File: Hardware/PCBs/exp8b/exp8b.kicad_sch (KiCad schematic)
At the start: 6 parts, among them J1 Conn_01x06_Female, J2 Conn_01x02_Female, U1 7410, U2 7410, U3 7410, U4 7400

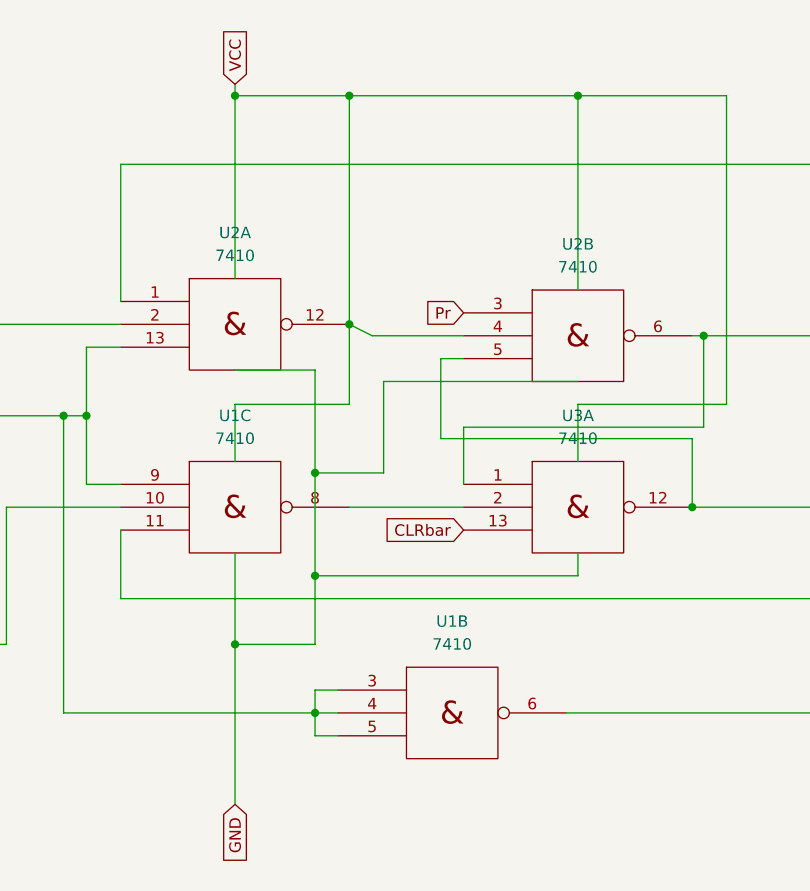
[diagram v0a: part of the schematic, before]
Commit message: Several PCBs updated
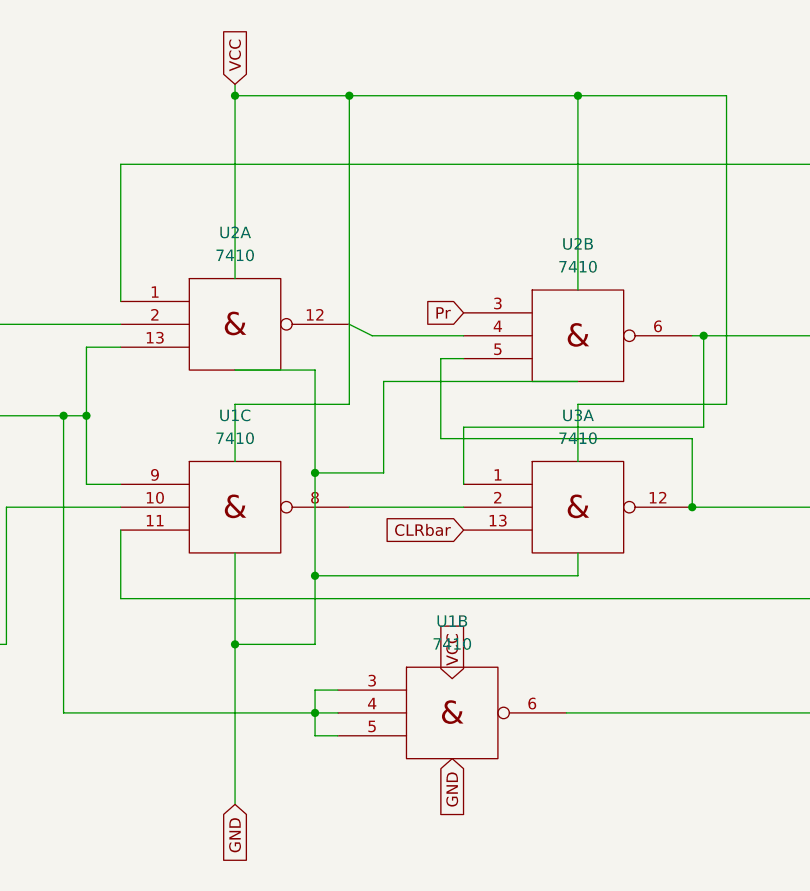
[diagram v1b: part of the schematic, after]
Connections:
- net Vcc: no longer U2.12, U2.4
- new net: U2.12, U2.4
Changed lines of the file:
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@@
   (junction (at 96.52 123.19) (diameter 0) (color 0 0 0 0)
   )
-  (junction (at 109.22 87.63) (diameter 0) (color 0 0 0 0)
-  )
   (junction (at 148.59 88.9) (diameter 0) (color 0 0 0 0)
   )
@@
     (stroke (width 0) (type default) (color 0 0 0 0))
   )
-  (wire (pts (xy 109.22 96.52) (xy 109.22 87.63))
-    (stroke (width 0) (type default) (color 0 0 0 0))
-  )
   (wire (pts (xy 209.55 101.6) (xy 209.55 106.68))
     (stroke (width 0) (type default) (color 0 0 0 0))
@@
     (stroke (width 0) (type default) (color 0 0 0 0))
   )
-  (wire (pts (xy 109.22 87.63) (xy 109.22 62.23))
+  (wire (pts (xy 109.22 62.23) (xy 109.22 96.52))
     (stroke (width 0) (type default) (color 0 0 0 0))
   )
@@
     )
   )
+  (global_label "VCC" (shape input) (at 120.65 127 90) (fields_autoplaced)
+    (effects (font (size 1.27 1.27)) (justify left))
+    (property "Intersheet References" "${INTERSHEET_REFS}" (id 0) (at 120.7294 120.9583 90)
+      (effects (font (size 1.27 1.27)) (justify left) hide)
+    )
+  )
   (global_label "Q" (shape input) (at 240.03 88.9 0) (fields_autoplaced)
     (effects (font (size 1.27 1.27)) (justify left))
@@
     )
   )
+  (global_label "GND" (shape input) (at 120.65 135.89 270) (fields_autoplaced)
+    (effects (font (size 1.27 1.27)) (justify right))
+    (property "Intersheet References" "${INTERSHEET_REFS}" (id 0) (at 120.7294 142.1736 90)
+      (effects (font (size 1.27 1.27)) (justify right) hide)
+    )
+  )
